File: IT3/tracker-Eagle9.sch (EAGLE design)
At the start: 91 parts, among them J1 THING_PLUS_PHYSICAL, Q1 2N3906, Q2 DMG6602SVT, Q3 DMG6602SVT, Q6 MMBT3906LT1SMD, Q7 DMG6602SVT, U1 ADXL343BCCZ-RL7, U2 FONA-800-BREAKOUTNOHOLE, U3 MP2155GQ-Z, U4 SPARKFUN-SWARM-M138NOTOPHOLE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

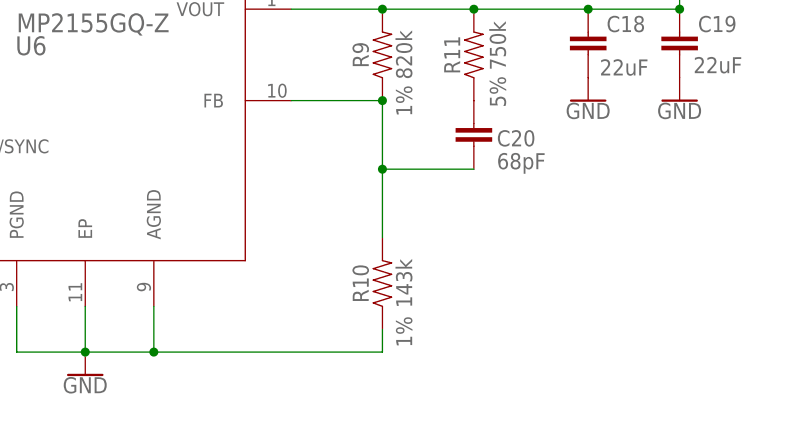
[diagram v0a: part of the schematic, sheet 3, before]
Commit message: Final silkscreen tweaks and generation of production files
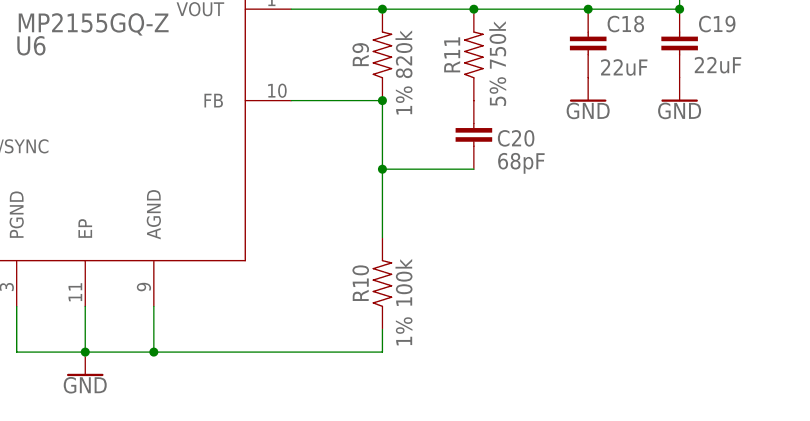
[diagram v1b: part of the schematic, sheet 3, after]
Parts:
- R10: value 143k -> 100k
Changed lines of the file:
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@@
 <attribute name="TOLERANCE" value="1%"/>
 </part>
-<part name="R10" library="SparkFun-Resistors" deviceset="RESISTOR" device="0603" value="143k">
+<part name="R10" library="SparkFun-Resistors" deviceset="RESISTOR" device="0603" value="100k">
 <attribute name="TOLERANCE" value="1%"/>
 </part>

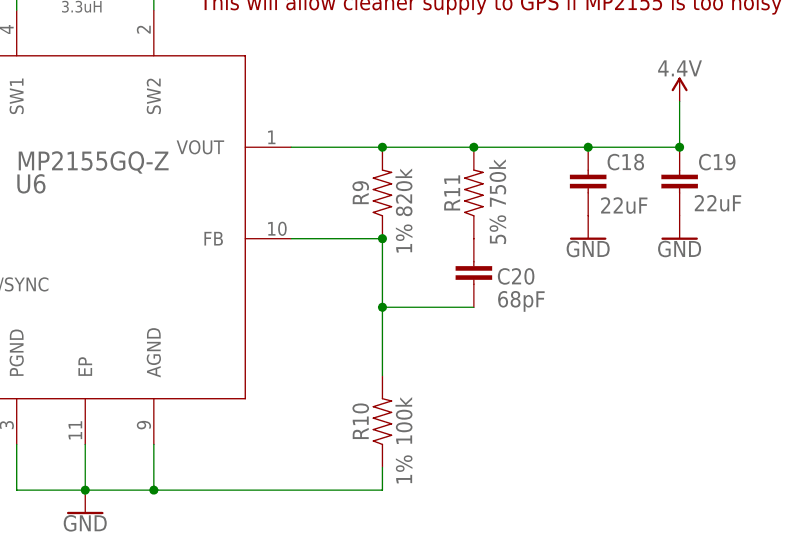
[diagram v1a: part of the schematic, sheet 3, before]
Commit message: Update 4V PSUvalues
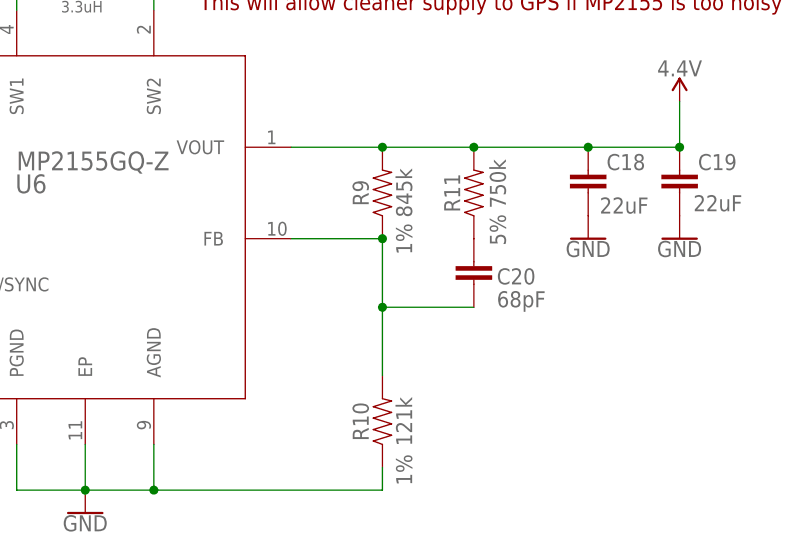
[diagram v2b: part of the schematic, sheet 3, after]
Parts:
- R10: value 100k -> 121k
- R9: value 820k -> 845k
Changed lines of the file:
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@@
 <attribute name="VOLTAGE_RATING" value="50V"/>
 </part>
-<part name="R9" library="SparkFun-Resistors" deviceset="RESISTOR" device="0603" value=" 820k">
+<part name="R9" library="SparkFun-Resistors" deviceset="RESISTOR" device="0603" value=" 845k">
 <attribute name="TOLERANCE" value="1%"/>
 </part>
-<part name="R10" library="SparkFun-Resistors" deviceset="RESISTOR" device="0603" value="100k">
+<part name="R10" library="SparkFun-Resistors" deviceset="RESISTOR" device="0603" value="121k">
 <attribute name="TOLERANCE" value="1%"/>
 </part>

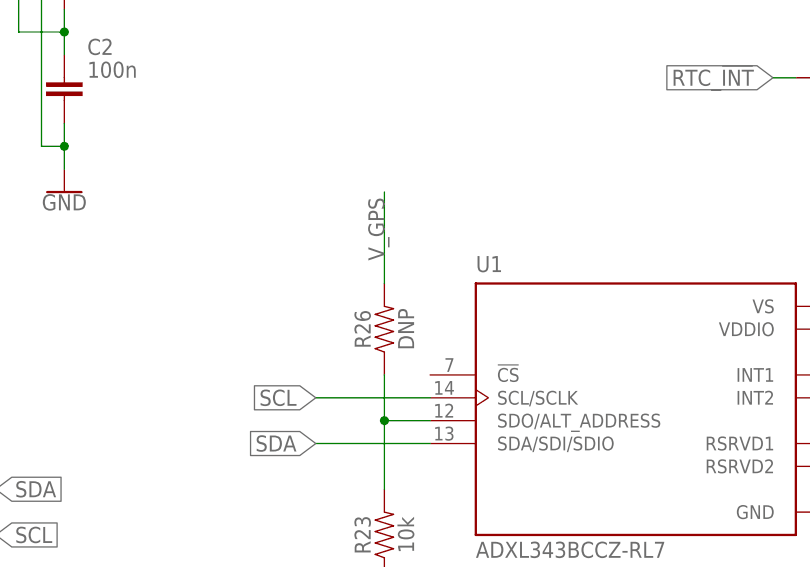
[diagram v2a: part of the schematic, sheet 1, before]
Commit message: Fixes for accelerometer CS pullup
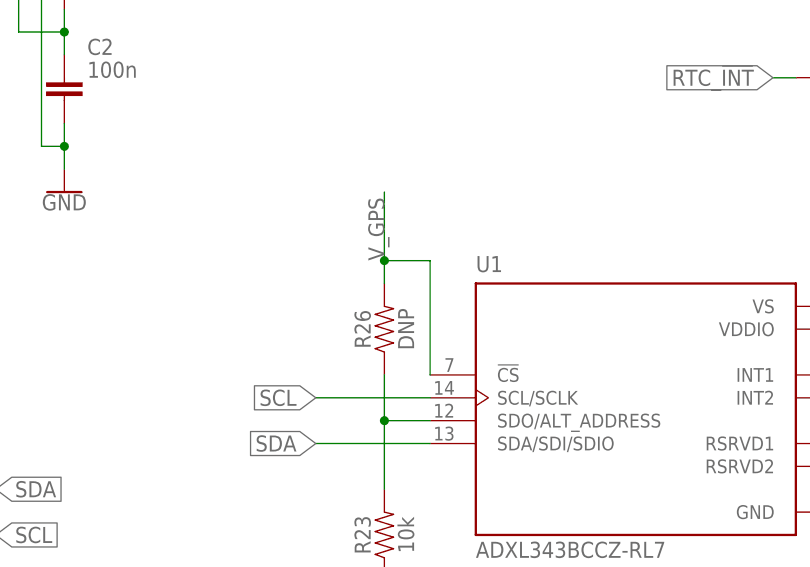
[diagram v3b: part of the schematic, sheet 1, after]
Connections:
- net V_GPS: now also U1.!CS
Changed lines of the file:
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@@
 </segment>
 <segment>
-<wire x1="129.54" y1="81.28" x2="129.54" y2="71.12" width="0.1524" layer="91"/>
+<wire x1="129.54" y1="81.28" x2="129.54" y2="73.66" width="0.1524" layer="91"/>
 <label x="129.54" y="73.66" size="1.778" layer="95" rot="R90"/>
 <pinref part="R26" gate="G$1" pin="2"/>
+<pinref part="U1" gate="G$1" pin="!CS"/>
+<wire x1="129.54" y1="73.66" x2="129.54" y2="71.12" width="0.1524" layer="91"/>
+<wire x1="134.62" y1="60.96" x2="134.62" y2="73.66" width="0.1524" layer="91"/>
+<wire x1="134.62" y1="73.66" x2="129.54" y2="73.66" width="0.1524" layer="91"/>
+<junction x="129.54" y="73.66"/>
 </segment>
 </net>
